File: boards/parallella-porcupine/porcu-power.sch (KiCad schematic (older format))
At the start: 11 parts, among them J10 CONN\\HDR\\P1\\1R04, J11 CONN\\HDR\\2MM\\2R07\\SHD, J12 CONN\\HDR\\P1\\1R02, J13 CONN\\HDR\\P1\\1R02, J14 CONN\\HDR\\P1\\2R15\\SHD, J5 CONN\\HDR\\P1\\1R08, J6 CONN\\HDR\\P1\\2R08, J7 CONN\\HDR\\P1\\2R08, J8 CONN\\HDR\\P1\\1R04, J9 CONN\\HDR\\P1\\1R04

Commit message: Schematic is stable, PCB mostly routed.
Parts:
- removed J14: CONN\\HDR\\P1\\2R15\\SHD, CONN_HDR_P1_2R15_SHD, symbol CONN\HDR\P1\2R15\SHD
- removed J5: CONN\\HDR\\P1\\1R08, CONN_HDR_P1_1R08, symbol CONN\HDR\P1\1R08
- removed J6, J7: CONN\\HDR\\P1\\2R08, CONN_HDR_P1_2R08, symbol CONN\HDR\P1\2R08
- added J14: CONN\\HDR\\P1\\2R15, CONN_HDR_P1_2R15, symbol CONN\HDR\P1\2R15
- added J6: CONN\\HDR\\P1\\2R04, CONN_HDR_P1_2R04, symbol CONN\HDR\P1\2R04
- added J7: CONN\\HDR\\2MM\\3R08, CONN_HDR_2MM_3R08, symbol CONN\HDR\2MM\3R08
- renumbered R1 to R9
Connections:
- wire segments 111 -> 103
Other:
- note added: "On the Parallella, ID pins are either 1k to ground or\n4.75k to Vdd. The default address is Y:1000 X:0010."
- note removed: "On the Parallella, ID pins are either 1k to ground or\n4.75k to Vdd. These headers will be arranged\nin 3 rows 0.1" apart to support jumpering in either \ndirection."
- moved on the sheet: J10, J11, J12, J13, J8, J9

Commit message: Completed design w/3-row XID/YID and various 4-pin IO connectors. Fixed page ordering, changed "Mfr" field to "Manufacturer" Will now re-do to combine all misc. functions onto a single 2xN connector.
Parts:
- removed R9: 1K, R_0805_HS, symbol R
- added R9: 1k00, R_0805_HS, symbol R\SMD0805\1PCT\1K00
- J10, J14, J7, J8, J9: MFR Sullins -> (none); Manufacturer (none) -> Sullins
- J11: MFR Molex -> (none); Manufacturer (none) -> Molex
- J12, J13: MFR 3M -> (none); Manufacturer (none) -> 3M
- J6: MFR FCI -> (none); Manufacturer (none) -> FCI
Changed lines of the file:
@@
 NoConn ~ 8600 3200
 $Comp
-L GND #PWR017
+L GND #PWR012
 U 1 1 538E9BA0
 P 8450 3950
-F 0 "#PWR017" H 8450 3950 30  0001 C CNN
+F 0 "#PWR012" H 8450 3950 30  0001 C CNN
 F 1 "GND" H 8450 3880 30  0001 C CNN
 F 2 "" H 8450 3950 60  0000 C CNN
@@
 Text Label 9400 3200 0    60   ~ 0
 3P3V
-$Comp
-L R R9
-U 1 1 538E9D4A
-P 11950 3450
-F 0 "R9" V 12030 3450 40  0000 C CNN
-F 1 "1K" V 11957 3451 40  0000 C CNN
-F 2 "R_0805_HS" V 11880 3450 30  0000 C CNN
-F 3 "" H 11950 3450 30  0000 C CNN
-	1    11950 3450
-	0    -1   -1   0
-$EndComp
 Wire Wire Line
 	9500 3300 9200 3300
@@
 NoConn ~ 9200 3800
 $Comp
-L GND #PWR018
+L GND #PWR013
 U 1 1 538E9E96
 P 12350 3550
-F 0 "#PWR018" H 12350 3550 30  0001 C CNN
+F 0 "#PWR013" H 12350 3550 30  0001 C CNN
 F 1 "GND" H 12350 3480 30  0001 C CNN
 F 2 "" H 12350 3550 60  0000 C CNN
@@
 1P8V
 $Comp
-L GND #PWR019
+L GND #PWR014
 U 1 1 538EAE9D
 P 13150 7200
-F 0 "#PWR019" H 13150 7200 30  0001 C CNN
+F 0 "#PWR014" H 13150 7200 30  0001 C CNN
 F 1 "GND" H 13150 7130 30  0001 C CNN
 F 2 "" H 13150 7200 60  0000 C CNN
@@
 NoConn ~ 12450 6500
 $Comp
-L GND #PWR020
+L GND #PWR015
 U 1 1 538EBE96
 P 7850 5950
-F 0 "#PWR020" H 7850 5950 30  0001 C CNN
+F 0 "#PWR015" H 7850 5950 30  0001 C CNN
 F 1 "GND" H 7850 5880 30  0001 C CNN
 F 2 "" H 7850 5950 60  0000 C CNN
@@
 3P3V
 $Comp
-L GND #PWR021
+L GND #PWR016
 U 1 1 538EC9A1
 P 7850 6750
-F 0 "#PWR021" H 7850 6750 30  0001 C CNN
+F 0 "#PWR016" H 7850 6750 30  0001 C CNN
 F 1 "GND" H 7850 6680 30  0001 C CNN
 F 2 "" H 7850 6750 60  0000 C CNN
@@
 	7950 7350 7700 7350
 $Comp
-L GND #PWR022
+L GND #PWR017
 U 1 1 538EC9B8
 P 7850 7550
-F 0 "#PWR022" H 7850 7550 30  0001 C CNN
+F 0 "#PWR017" H 7850 7550 30  0001 C CNN
 F 1 "GND" H 7850 7480 30  0001 C CNN
 F 2 "" H 7850 7550 60  0000 C CNN
@@
 3P3V
 $Comp
-L GND #PWR023
+L GND #PWR018
 U 1 1 538FBBE6
 P 12400 4550
-F 0 "#PWR023" H 12400 4550 30  0001 C CNN
+F 0 "#PWR018" H 12400 4550 30  0001 C CNN
 F 1 "GND" H 12400 4480 30  0001 C CNN
 F 2 "" H 12400 4550 60  0000 C CNN
@@
 F 3 "" H 8900 4000 60  0001 C CNN
 F 4 "0878311420" H 8900 3950 50  0000 C CNN "MFRPN"
-F 5 "Molex" H 8900 4150 50  0001 C CNN "MFR"
+F 5 "Molex" H 8900 4150 50  0001 C CNN "Manufacturer"
 	1    8900 3500
 	1    0    0    -1
@@
 F 3 "" H 12000 3450 60  0001 C CNN
 F 4 "961102-6404-AR" H 12150 3400 50  0000 C CNN "MFRPN"
-F 5 "3M" H 12000 3600 50  0001 C CNN "MFR"
+F 5 "3M" H 12000 3600 50  0001 C CNN "Manufacturer"
 	1    12000 3250
 	1    0    0    -1
@@
 F 3 "" H 12000 4650 60  0001 C CNN
 F 4 "961102-6404-AR" H 12150 4600 50  0000 C CNN "MFRPN"
-F 5 "3M" H 12000 4800 50  0001 C CNN "MFR"
+F 5 "3M" H 12000 4800 50  0001 C CNN "Manufacturer"
 	1    12000 4450
 	1    0    0    -1
@@
 F 3 "" H 8250 6050 60  0001 C CNN
 F 4 "PRPC004SAAN-RC" H 8400 6000 50  0000 C CNN "MFRPN"
-F 5 "Sullins" H 8250 6200 50  0001 C CNN "MFR"
+F 5 "Sullins" H 8250 6200 50  0001 C CNN "Manufacturer"
 	1    8200 5700
 	1    0    0    -1
@@
 F 3 "" H 8250 6850 60  0001 C CNN
 F 4 "PRPC004SAAN-RC" H 8400 6800 50  0000 C CNN "MFRPN"
-F 5 "Sullins" H 8250 7000 50  0001 C CNN "MFR"
+F 5 "Sullins" H 8250 7000 50  0001 C CNN "Manufacturer"
 	1    8200 6500
 	1    0    0    -1
@@
 F 3 "" H 8250 7650 60  0001 C CNN
 F 4 "PRPC004SAAN-RC" H 8400 7600 50  0000 C CNN "MFRPN"
-F 5 "Sullins" H 8250 7800 50  0001 C CNN "MFR"
+F 5 "Sullins" H 8250 7800 50  0001 C CNN "Manufacturer"
 	1    8200 7300
 	1    0    0    -1
@@
 F 3 "" H 12750 7300 60  0001 C CNN
 F 4 "PRPC015DAAN-RC" H 12900 7250 50  0000 C CNN "MFRPN"
-F 5 "Sullins" H 12750 7450 50  0001 C CNN "MFR"
+F 5 "Sullins" H 12750 7450 50  0001 C CNN "Manufacturer"
 F 6 "DNI" H 13400 7100 60  0000 C CNN "DNI"
 	1    12750 6400
@@
 F 3 "" H 4600 6700 60  0001 C CNN
 F 4 "67997-208HLF" H 4800 6650 50  0000 C CNN "MFRPN"
-F 5 "FCI" H 4600 6850 50  0001 C CNN "MFR"
+F 5 "FCI" H 4600 6850 50  0001 C CNN "Manufacturer"
 	1    4600 6350
 	1    0    0    -1
 $EndComp
 $Comp
-L GND #PWR024
+L GND #PWR019
 U 1 1 538ED07C
 P 5000 6600
-F 0 "#PWR024" H 5000 6600 30  0001 C CNN
+F 0 "#PWR019" H 5000 6600 30  0001 C CNN
 F 1 "GND" H 5000 6530 30  0001 C CNN
 F 2 "" H 5000 6600 60  0000 C CNN
@@
 F 3 "" H 6000 3250 60  0001 C CNN
 F 4 "NRPN082PAEN-RC_+_NRPN081PAEN-RC" H 6200 3200 50  0000 C CNN "MFRPN"
-F 5 "Sullins" H 6000 3400 50  0001 C CNN "MFR"
+F 5 "Sullins" H 6000 3400 50  0001 C CNN "Manufacturer"
 	1    6000 2750
 	1    0    0    -1
@@
 Connection ~ 6500 2650
 $Comp
-L GND #PWR025
+L GND #PWR020
 U 1 1 5398C452
 P 6500 4100
-F 0 "#PWR025" H 6500 4100 30  0001 C CNN
+F 0 "#PWR020" H 6500 4100 30  0001 C CNN
 F 1 "GND" H 6500 4030 30  0001 C CNN
 F 2 "" H 6500 4100 60  0000 C CNN
@@
 Connection ~ 5600 2450
 Connection ~ 6500 3850
+$Comp
+L R\SMD0805\1PCT\1K00 R9
+U 1 1 539F6C71
+P 11950 3450
+F 0 "R9" V 12050 3450 40  0000 C CNN
+F 1 "1k00" V 11957 3451 40  0000 C CNN
+F 2 "R_0805_HS" V 11880 3450 30  0000 C CNN
+F 3 "" V 12030 3450 30  0000 C CNN
+F 4 "RC0805FR-071KL" V 11800 3550 60  0000 C CNN "MFRPN"
+F 5 "Yageo" V 12150 3450 60  0001 C CNN "Manufacturer"
+	1    11950 3450
+	0    -1   -1   0
+$EndComp
 $EndSCHEMATC

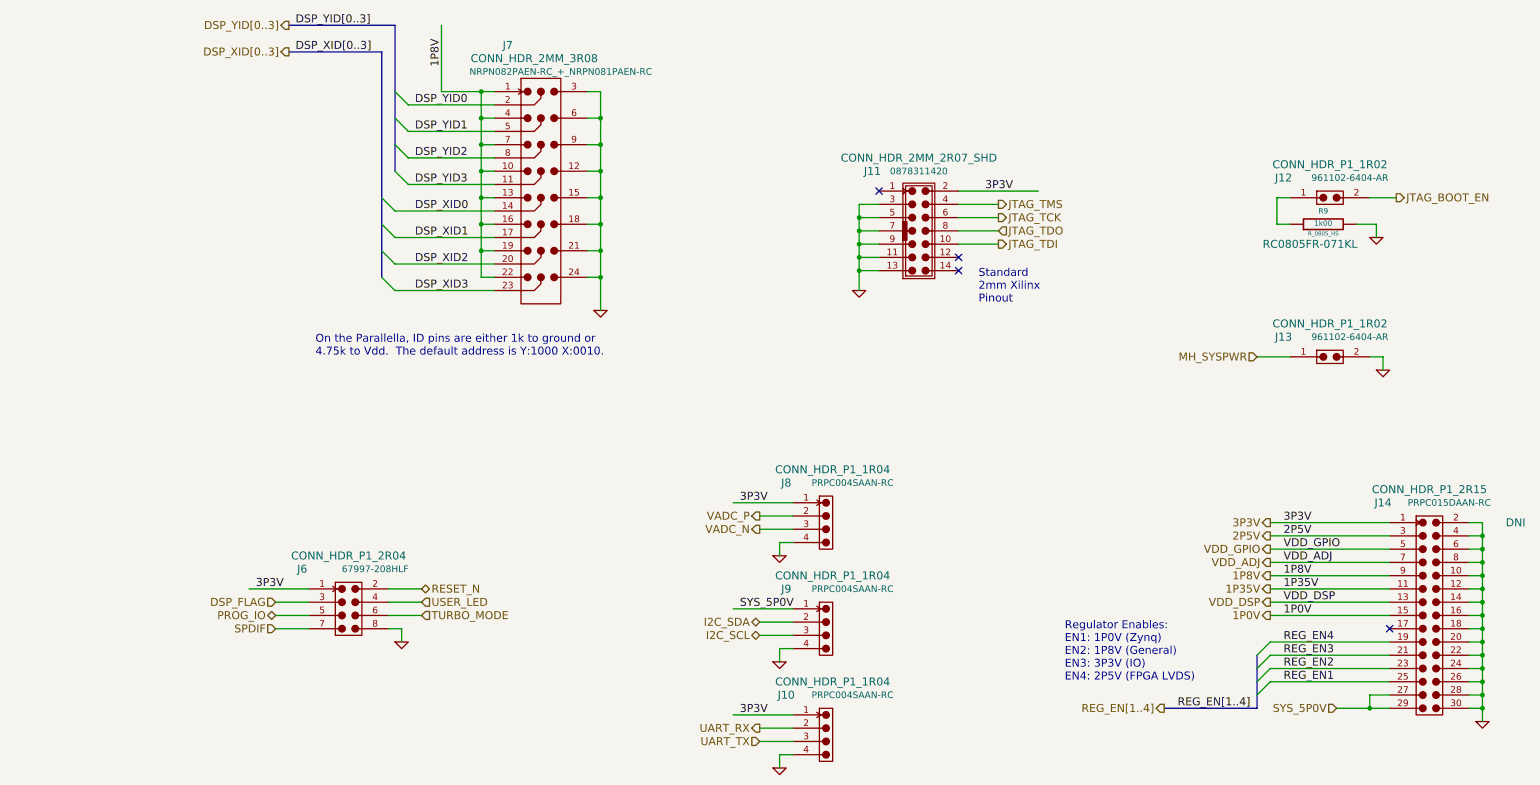
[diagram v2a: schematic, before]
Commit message: Changed to a single header for all the PEC_POWER/misc. stuff. Added 3D models for shrouded & right-angle connectors.
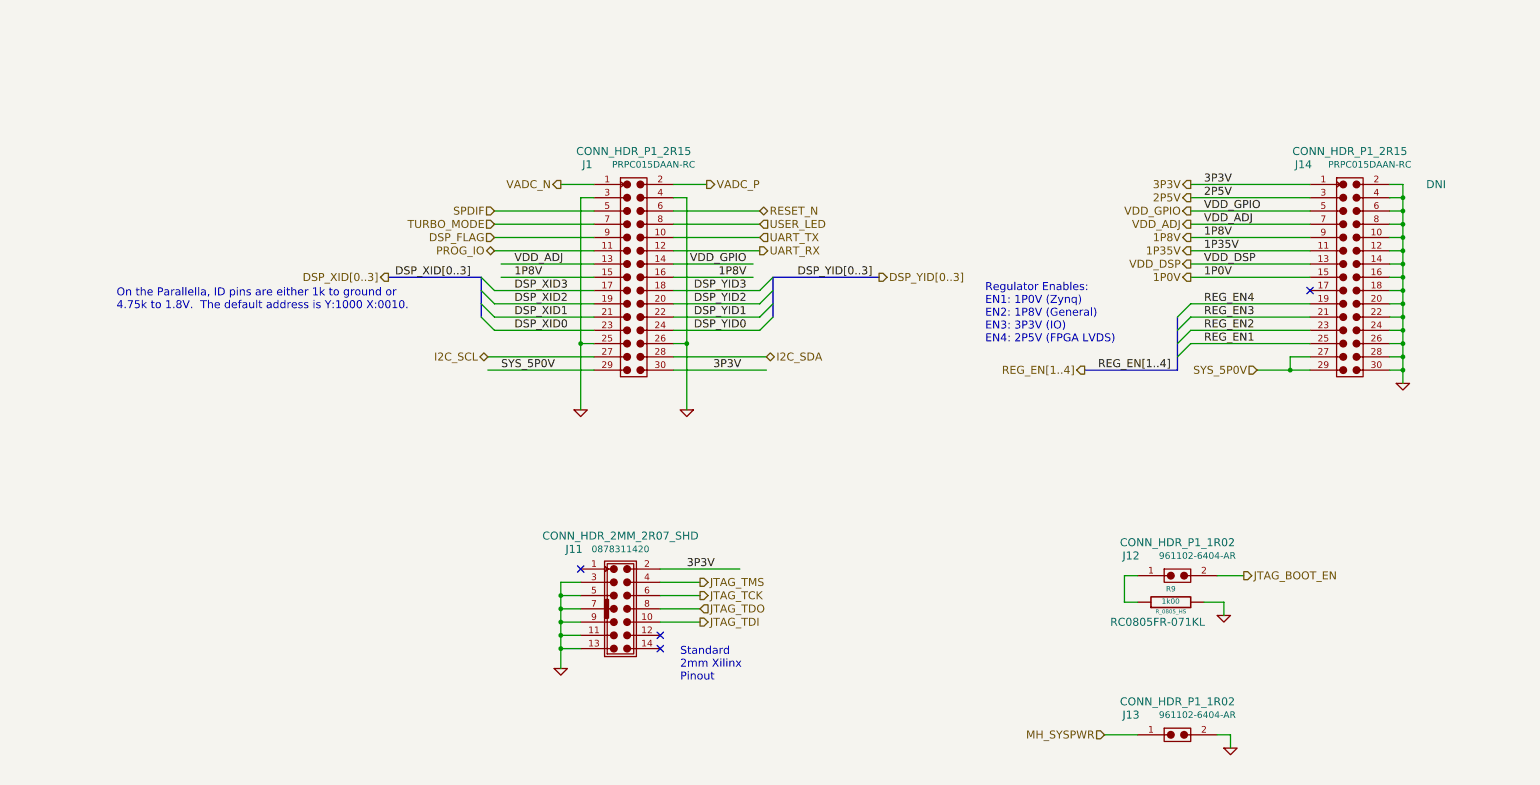
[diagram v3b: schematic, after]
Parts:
- removed J10, J8, J9: CONN\\HDR\\P1\\1R04, CONN_HDR_P1_1R04, symbol CONN\HDR\P1\1R04
- removed J6: CONN\\HDR\\P1\\2R04, CONN_HDR_P1_2R04, symbol CONN\HDR\P1\2R04
- removed J7: CONN\\HDR\\2MM\\3R08, CONN_HDR_2MM_3R08, symbol CONN\HDR\2MM\3R08
- added J1: CONN\\HDR\\P1\\2R15, CONN_HDR_P1_2R15, symbol CONN\HDR\P1\2R15
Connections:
- wire segments 103 -> 84
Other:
- note added: "On the Parallella, ID pins are either 1k to ground or\n4.75k to 1.8V. The default address is Y:1000 X:0010."
- note removed: "On the Parallella, ID pins are either 1k to ground or\n4.75k to Vdd. The default address is Y:1000 X:0010."
- moved on the sheet: J11, J12, J13, J14, R9

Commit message: Ready for full review.
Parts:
- removed J12: CONN\\HDR\\P1\\1R02, CONN_HDR_P1_1R02, symbol CONN\HDR\P1\1R02
- removed R9: 1k00, R_0805_HS, symbol R\SMD0805\1PCT\1K00
- renumbered J11 to J1, J1 to J2, J14 to J3, J13 to J4
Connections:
- net labels added: SPARE
- wire segments 84 -> 81
- no-connect marks 4 -> 3
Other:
- note added: "Regulator Enables:\nEN4: 2P5V (FPGA LVDS)\nEN3: 3P3V (IO)\nEN2: 1P8V (General)\nEN1: 1P0V (Zynq)"
- note removed: "Regulator Enables:\nEN1: 1P0V (Zynq)\nEN2: 1P8V (General)\nEN3: 3P3V (IO)\nEN4: 2P5V (FPGA LVDS)"
- moved on the sheet: J1, J2, J4

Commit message: Porcupine Version 2.
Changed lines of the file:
@@
 LIBS:valves
 LIBS:porcupine-cache
-EELAYER 24 0
+EELAYER 25 0
 EELAYER END
 $Descr B 17000 11000
 encoding utf-8
-Sheet 7 10
-Title "Parallella Breakout Daughtercard"
-Date "19 Jun 2014"
-Rev "*"
+Sheet 7 11
+Title "Parallella Breakout Daughtercard, Ver. 2"
+Date "17 feb 2015"
+Rev "A"
 Comp "Adapteva, Inc., 1666 Massachusetts Ave., Lexington, MA, 02420"
-Comment1 "including JTAG"
+Comment1 "Porcupine Top Level"
 Comment2 "Various Power connectors and Jumpers"
 Comment3 ""
@@
 Text Notes 2050 4400 0    60   ~ 0
 On the Parallella, ID pins are either 1k to ground or\n4.75k to 1.8V.  The default address is Y:1000 X:0010.
-Text Notes 9400 4350 0    60   ~ 0
+Text Notes 9250 4000 0    60   ~ 0
 Regulator Enables:\nEN4: 2P5V (FPGA LVDS)\nEN3: 3P3V (IO)\nEN2: 1P8V (General)\nEN1: 1P0V (Zynq)
 Entry Wire Line
